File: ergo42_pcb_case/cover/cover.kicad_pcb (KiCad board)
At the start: 2 copper layers, 78.2 x 23.6 mm, 6 parts

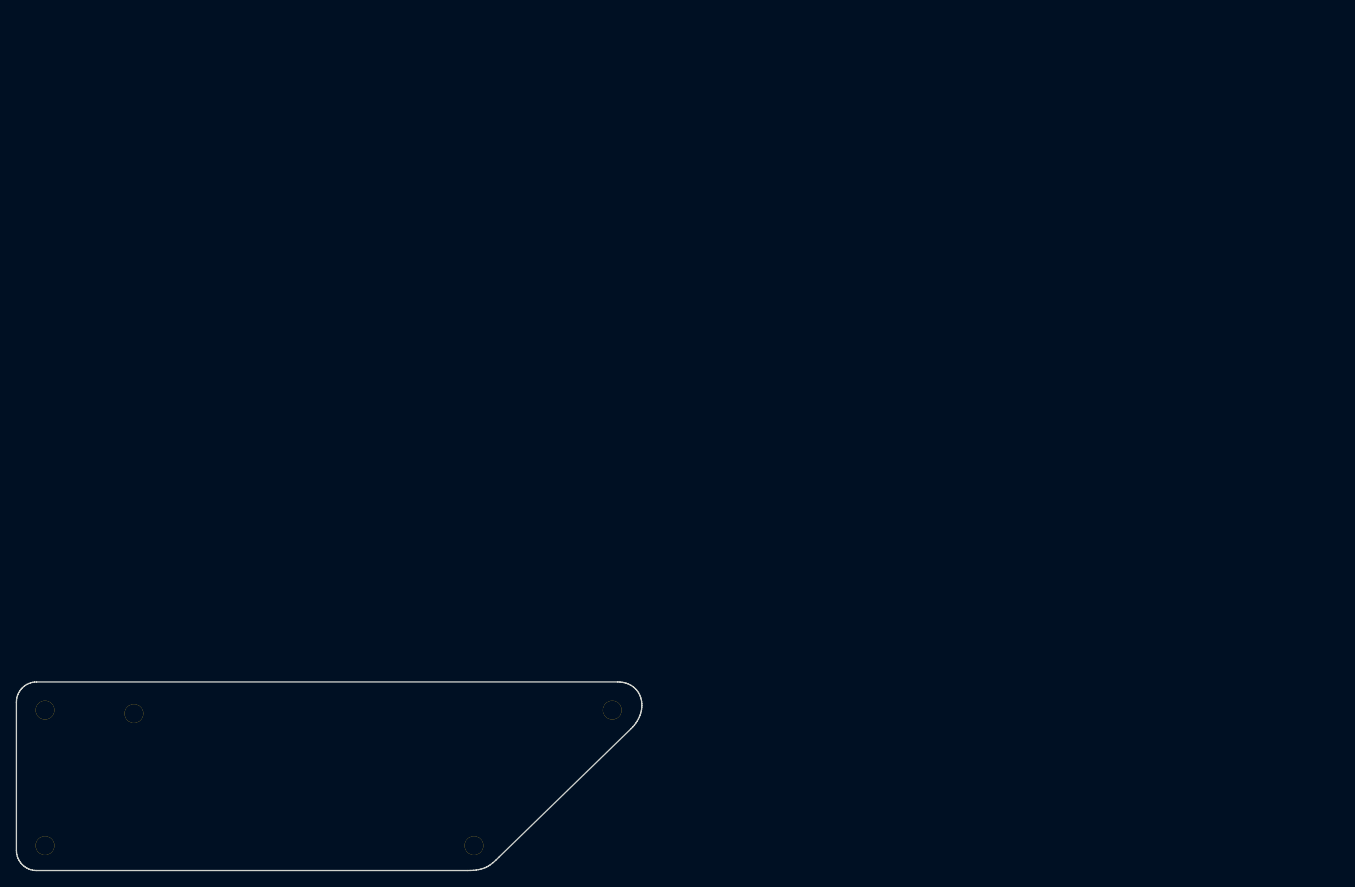
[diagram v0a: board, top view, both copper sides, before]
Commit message: FreeCAD to KiCAD approach
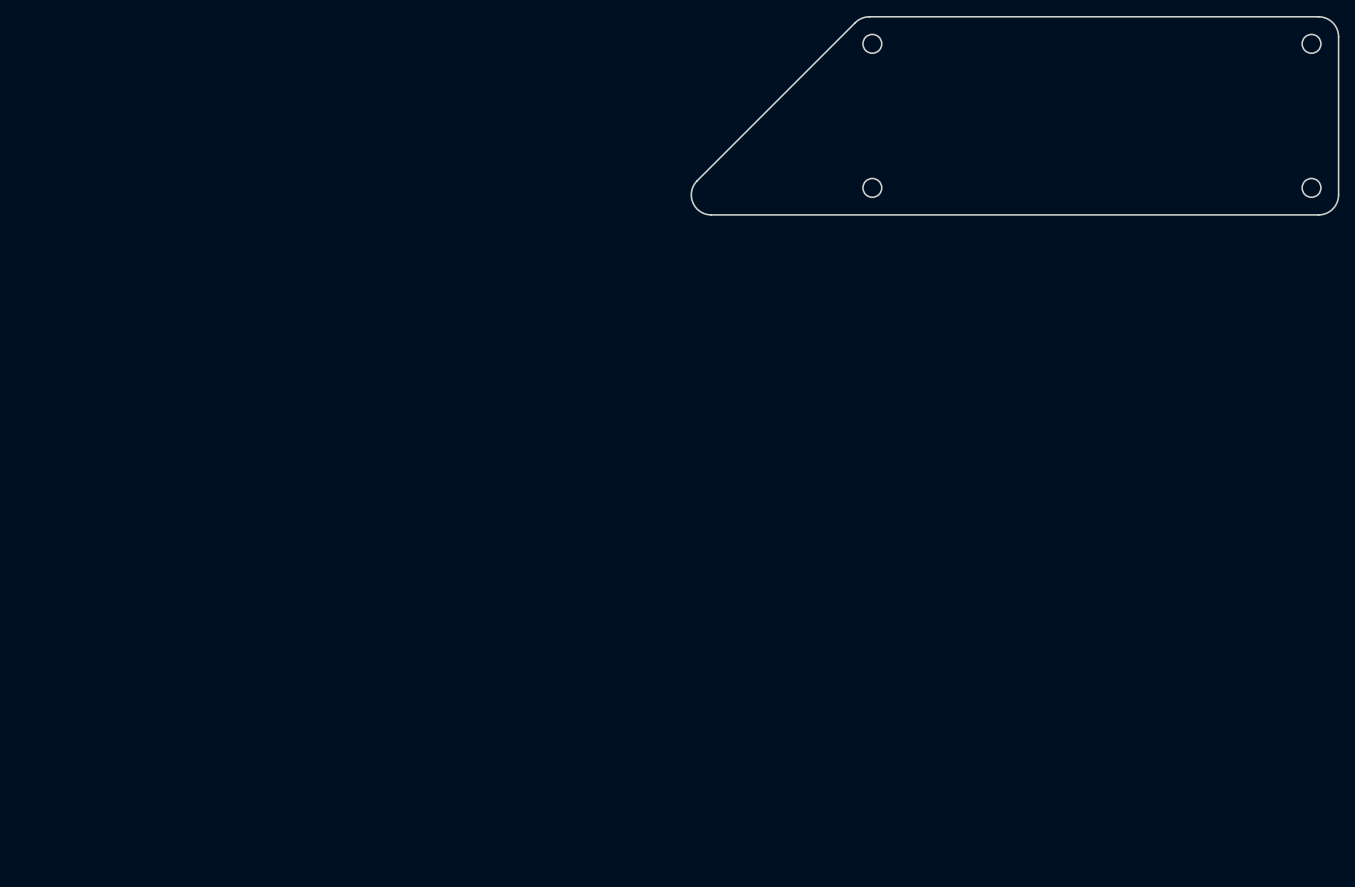
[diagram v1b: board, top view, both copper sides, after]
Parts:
- removed ? (x5): , Wire_Pads:SolderWirePad_single_0-8mmDrill
- removed G***: LOGO, LOGO
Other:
- board size 78.2 x 23.6 mm -> 80.9 x 24.8 mm
- net class Default: via_dia 0.6 -> 0.8
- rule pad_to_mask_clearance: 0.2 -> 0.051
